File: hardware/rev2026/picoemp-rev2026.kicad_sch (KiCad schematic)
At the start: 47 parts, among them J1 Header 7, J2 1x2_Pin_Header, J3 BG306-02-A-2-0400-L-G, J4 Header 2, J5 Header 4, J6 EDGE-SMA, Q1 LDA111STR, Q2 RGT16BM65DTL, Q3 AO3422, Q4 AO3422, SW1 KSC741J LFS, SW2 KSC741J LFS, SW3 TL3301AF160QJ, T1 ATB322524, T2 ATB322524, U1 SC0915

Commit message: Restore upstream designators and fix header pitch to 2.54mm
The port had P1/P2/P3 replaced by 1.00mm and 1.27mm headers - a 2-2.5x
pitch error on every one. Restoring upstream designators keeps
BUILD-DRAWING-REV04.PDF and the README BOM explainer applicable.

Renames (verified to move zero netlist connections via before/after
membership comparison): LED1/2/3 -> D6/D8/D9, J1/J4/J5 (headers) ->
P1/P2/P3, J6 (SMA) -> J1. Headers get 2.54mm-pitch footprints. Cleared
stale DNP/in_bom=no flags on P1/P2/P3/J2/J3 left over from the
half-finished port.

SW1-3 get footprints: SW1/SW2 share KiCad's stock
Button_Switch_SMD:SW_Push_1P1T_NO_CK_KSC7xxJ land (C&K KSC741JLFS).
SW3 (E-Switch TL3301AF160QJ) gets its own project-local footprint
instead: despite upstream calling it a "shared footprint" part, the
datasheets disagree materially (4.50mm pin pitch vs the KSC7xxJ land's
4.00mm, a 12.5% mismatch).

Backfills the last three missing MPNs (D6/D9 -> APT1608SURCK, the
DigiKey-named substitute for the obsolete APT1608SRCPRV; SW1/SW2 ->
KSC741JLFS; SW3 -> TL3301AF160QJ) with Manufacturer/DigiKey via the
kicad-happy bom skill's edit_properties.py.

Co-Authored-By: Claude Opus 5 <noreply@anthropic.com>
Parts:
- D6: renamed from LED1; DigiKey (none) -> 754-1123-1-ND; MPN (none) -> APT1608SURCK; Manufacturer (none) -> Kingbright
- D9: renamed from LED3; DigiKey (none) -> 754-1123-1-ND; MPN (none) -> APT1608SURCK; Manufacturer (none) -> Kingbright
- J2, J3: now fitted; now in the parts list
- P1: renamed from J1; footprint Connector_PinHeader_1.00mm:PinHeader_1x07_P1.00mm_Vertical -> Connector_PinHeader_2.54mm:PinHeader_1x07_P2.54mm_Vertical; now fitted; now in the parts list
- P2: renamed from J4; footprint Connector_PinHeader_1.27mm:PinHeader_1x02_P1.27mm_Vertical -> Connector_PinHeader_2.54mm:PinHeader_1x02_P2.54mm_Vertical; now fitted; now in the parts list
- P3: renamed from J5; footprint Connector_PinHeader_1.00mm:PinHeader_1x04_P1.00mm_Vertical -> Connector_PinHeader_2.54mm:PinHeader_1x04_P2.54mm_Vertical; now fitted; now in the parts list
- SW1, SW2: footprint (none) -> Button_Switch_SMD:SW_Push_1P1T_NO_CK_KSC7xxJ; DigiKey (none) -> CKN10309CT-ND; MPN (none) -> KSC741JLFS; Manufacturer (none) -> C&K
- SW3: footprint (none) -> picoemp:SW_Push_ESwitch_TL3301AJ; DigiKey (none) -> EG4374CT-ND; MPN (none) -> TL3301AF160QJ; Manufacturer (none) -> E-Switch
- renumbered LED2 to D8, J6 to J1
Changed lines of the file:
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@@
 		(body_style 1)
 		(exclude_from_sim no)
-		(in_bom no)
+		(in_bom yes)
 		(on_board yes)
 		(in_pos_files yes)
-		(dnp yes)
+		(dnp no)
 		(fields_autoplaced yes)
-		(property "Reference" "J1"
+		(property "Reference" "P1"
 			(at 66.675 76.2 0)
 			(show_name no)
@@
 			)
 		)
-		(property "Footprint" "Connector_PinHeader_1.00mm:PinHeader_1x07_P1.00mm_Vertical"
+		(property "Footprint" "Connector_PinHeader_2.54mm:PinHeader_1x07_P2.54mm_Vertical"
 			(at 66.04 86.36 0)
 			(hide yes)
@@
 			(project "ChipShouter-Pico"
 				(path "/2587a454-e9b8-4dd2-940e-91a5ec62d2c9"
-					(reference "J1")
+					(reference "P1")
 					(unit 1)
 				)
@@
 			)
 		)
-		(property "Footprint" ""
+		(property "Footprint" "picoemp:SW_Push_ESwitch_TL3301AJ"
 			(at 347.98 215.9 0)
 			(hide yes)
@@
 			)
 		)
+		(property "DigiKey" "EG4374CT-ND" (at 0 0 0)
+			(effects
+				(font
+					(size 1.27 1.27)
+				)
+				(hide yes)
+			)
+		)
+		(property "Manufacturer" "E-Switch" (at 0 0 0)
+			(effects
+				(font
+					(size 1.27 1.27)
+				)
+				(hide yes)
+			)
+		)
+		(property "MPN" "TL3301AF160QJ" (at 0 0 0)
+			(effects
+				(font
+					(size 1.27 1.27)
+				)
+				(hide yes)
+			)
+		)
 		(pin "1"
 		)
@@
 			)
 		)
-		(property "Footprint" ""
+		(property "Footprint" "Button_Switch_SMD:SW_Push_1P1T_NO_CK_KSC7xxJ"
 			(at 83.82 148.59 0)
 			(hide yes)
@@
 			)
 		)
+		(property "DigiKey" "CKN10309CT-ND" (at 0 0 0)
+			(effects
+				(font
+					(size 1.27 1.27)
+				)
+				(hide yes)
+			)
+		)
+		(property "Manufacturer" "C&K" (at 0 0 0)
+			(effects
+				(font
+					(size 1.27 1.27)
+				)
+				(hide yes)
+			)
+		)
+		(property "MPN" "KSC741JLFS" (at 0 0 0)
+			(effects
+				(font
+					(size 1.27 1.27)
+				)
+				(hide yes)
+			)
+		)
 		(pin "2"
 		)
@@
 			)
 		)
-		(property "Footprint" ""
+		(property "Footprint" "Button_Switch_SMD:SW_Push_1P1T_NO_CK_KSC7xxJ"
 			(at 238.76 127 0)
 			(hide yes)
@@
 			)
 		)
+		(property "DigiKey" "CKN10309CT-ND" (at 0 0 0)
+			(effects
+				(font
+					(size 1.27 1.27)
+				)
+				(hide yes)
+			)
+		)
+		(property "Manufacturer" "C&K" (at 0 0 0)
+			(effects
+				(font
+					(size 1.27 1.27)
+				)
+				(hide yes)
+			)
+		)
+		(property "MPN" "KSC741JLFS" (at 0 0 0)
+			(effects
+				(font
+					(size 1.27 1.27)
+				)
+				(hide yes)
+			)
+		)
 		(pin "1"
 		)
@@
 		(dnp no)
 		(fields_autoplaced yes)
-		(property "Reference" "LED3"
+		(property "Reference" "D9"
 			(at 235.2675 106.68 0)
 			(show_name no)
@@
 			)
 		)
+		(property "DigiKey" "754-1123-1-ND" (at 0 0 0)
+			(effects
+				(font
+					(size 1.27 1.27)
+				)
+				(hide yes)
+			)
+		)
+		(property "Manufacturer" "Kingbright" (at 0 0 0)
+			(effects
+				(font
+					(size 1.27 1.27)
+				)
+				(hide yes)
+			)
+		)
+		(property "MPN" "APT1608SURCK" (at 0 0 0)
+			(effects
+				(font
+					(size 1.27 1.27)
+				)
+				(hide yes)
+			)
+		)
 		(pin "2"
 		)
@@
 			(project "ChipShouter-Pico"
 				(path "/2587a454-e9b8-4dd2-940e-91a5ec62d2c9"
-					(reference "LED3")
+					(reference "D9")
 					(unit 1)
 				)
@@
 		(dnp no)
 		(fields_autoplaced yes)
-		(property "Reference" "LED2"
+		(property "Reference" "D8"
 			(at 64.4525 125.73 0)
 			(show_name no)
@@
 			(project "ChipShouter-Pico"
 				(path "/2587a454-e9b8-4dd2-940e-91a5ec62d2c9"
-					(reference "LED2")
+					(reference "D8")
 					(unit 1)
 				)
@@
 		(dnp no)
 		(fields_autoplaced yes)
-		(property "Reference" "LED1"
+		(property "Reference" "D6"
 			(at 64.4525 110.49 0)
 			(show_name no)
@@
 			)
 		)
+		(property "DigiKey" "754-1123-1-ND" (at 0 0 0)
+			(effects
+				(font
+					(size 1.27 1.27)
+				)
+				(hide yes)
+			)
+		)
+		(property "Manufacturer" "Kingbright" (at 0 0 0)
+			(effects
+				(font
+					(size 1.27 1.27)
+				)
+				(hide yes)
+			)
+		)
+		(property "MPN" "APT1608SURCK" (at 0 0 0)
+			(effects
+				(font
+					(size 1.27 1.27)
+				)
+				(hide yes)
+			)
+		)
 		(pin "2"
 		)
@@
 			(project "ChipShouter-Pico"
 				(path "/2587a454-e9b8-4dd2-940e-91a5ec62d2c9"
-					(reference "LED1")
+					(reference "D6")
 					(unit 1)
 				)
@@
 		(body_style 1)
 		(exclude_from_sim no)
-		(in_bom no)
+		(in_bom yes)
 		(on_board yes)
 		(in_pos_files yes)
-		(dnp yes)
+		(dnp no)
 		(fields_autoplaced yes)
-		(property "Reference" "J4"
+		(property "Reference" "P2"
 			(at 59.69 208.2801 0)
 			(hide yes)
@@
 			)
 		)
-		(property "Footprint" "Connector_PinHeader_1.27mm:PinHeader_1x02_P1.27mm_Vertical"
+		(property "Footprint" "Connector_PinHeader_2.54mm:PinHeader_1x02_P2.54mm_Vertical"
 			(at 58.42 205.74 0)
 			(hide yes)
@@
 			(project "ChipShouter-Pico"
 				(path "/2587a454-e9b8-4dd2-940e-91a5ec62d2c9"
-					(reference "J4")
+					(reference "P2")
 					(unit 1)
 				)
@@
 		(body_style 1)
 		(exclude_from_sim no)
-		(in_bom no)
+		(in_bom yes)
 		(on_board yes)
 		(in_pos_files yes)
-		(dnp yes)
+		(dnp no)
 		(fields_autoplaced yes)
 		(property "Reference" "J2"
@@
 		(dnp no)
 		(fields_autoplaced yes)
-		(property "Reference" "J6"
+		(property "Reference" "J1"
 			(at 420.624 270.51 90)
 			(show_name no)
@@
 			(project "ChipShouter-Pico"
 				(path "/2587a454-e9b8-4dd2-940e-91a5ec62d2c9"
-					(reference "J6")
+					(reference "J1")
 					(unit 1)
 				)
@@
 		(body_style 1)
 		(exclude_from_sim no)
-		(in_bom no)
+		(in_bom yes)
 		(on_board yes)
 		(in_pos_files yes)
-		(dnp yes)
+		(dnp no)
 		(fields_autoplaced yes)
 		(property "Reference" "J3"
@@
 		(body_style 1)
 		(exclude_from_sim no)
-		(in_bom no)
+		(in_bom yes)
 		(on_board yes)
 		(in_pos_files yes)
-		(dnp yes)
+		(dnp no)
 		(fields_autoplaced yes)
-		(property "Reference" "J5"
+		(property "Reference" "P3"
 			(at 99.06 210.8201 0)
 			(hide yes)
@@
 			)
 		)
-		(property "Footprint" "Connector_PinHeader_1.00mm:PinHeader_1x04_P1.00mm_Vertical"
+		(property "Footprint" "Connector_PinHeader_2.54mm:PinHeader_1x04_P2.54mm_Vertical"
 			(at 97.79 208.28 0)
 			(hide yes)
@@
 			(project "ChipShouter-Pico"
 				(path "/2587a454-e9b8-4dd2-940e-91a5ec62d2c9"
-					(reference "J5")
+					(reference "P3")
 					(unit 1)
 				)

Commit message: Add buffered trigger front-end, widen J3, gate on ERC and netlist parity
Trigger input gains a 74LVC1G17 Schmitt buffer (5.5V tolerant), series
and pulldown resistors, and a DNP bypass. J3 moves to 5.08mm: its
2.07mm pad gap failed IEC 60664-1 creepage at ~600V and the BG306's
500VAC rating is a proof test, not a working rating.

- U2 = Nexperia 74LVC1G17GV,125 (SOT-23-5), pinout verified against both
  the Nexperia and TI datasheets (1=NC, 2=A, 3=GND, 4=Y, 5=VCC).
- J3 = Phoenix Contact MKDS 1,5/2-5.08 terminal block (DigiKey 277-1263-ND).
- Pre-existing GND/AGND pin_to_pin ERC error resolved via a UUID-targeted
  erc_exclusions entry in the project file (not a net-tie or global
  severity change).
- 48 tests passing (0 failed); kicad-cli sch erc --severity-error
  --exit-code-violations exits 0.

Co-Authored-By: Claude Opus 5 <noreply@anthropic.com>
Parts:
- added C6: 100n, Capacitor_SMD:C_0603_1608Metric, symbol Device:C_Small
- added J4: EDGE-SMA, Connector_Coaxial:SMA_Amphenol_132289_EdgeMount, symbol Connector:Conn_Coaxial_Power
- added R14: 100R, Resistor_SMD:R_0603_1608Metric, symbol Device:R_Small
- added R15: 10k, Resistor_SMD:R_0603_1608Metric, symbol Device:R_Small
- added R16: 0R, Resistor_SMD:R_0603_1608Metric, symbol Device:R_Small
- added U2: 74LVC1G17, Package_TO_SOT_SMD:SOT-23-5, symbol 74xGxx:74LVC1G17
- J3: value BG306-02-A-2-0400-L-G -> MKDS 1,5/2-5.08; footprint (none) -> TerminalBlock_Phoenix:TerminalBlock_Phoenix_MKDS-1,5-2-5.08_1x02_P5.08mm_Horizontal; BOM Comments (none) -> HV calibration tap. Milled slot between pads - see spec sec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; DigiKey (none) -> 277-1263-ND; MPN (none) -> 1715721; Manufacturer (none) -> Phoenix Contact
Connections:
- net +3V3: now also C6.1, U2.5 (VCC)
- net GND: now also C6.2, J4.2 (Ext), R15.2, U2.3 (GND)
- net GP0: now reaches U1.1 (GPIO0)
- net GP0: now also R16.2, U2.4; no longer P1.1 (Pin_1)
- new net TRIG_BUF: R14.2, R15.1, R16.1, U2.2
- new net TRIG_IN: J4.1 (In), P1.1 (Pin_1), R14.1

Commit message: Lay out the trigger front-end, add HV netclass, start the board
Schematic: trigger front-end placed and wired. Verified against the
exported netlist - /TRIG_IN {P1.1, J4.1, R14.1}, /TRIG_BUF {R14.2,
R15.1, R16.1, U2.2}, /GP0 {R16.2, U1.1, U2.4} with no P1.1 member,
U2.5 on +3V3 and U2.3 on GND. ERC exits 0, 54 tests pass.

Board setup: min_clearance 0.0 -> 0.2 (it was enforcing nothing on a
board that generates ~500V), plus an HV netclass at 0.75mm assigned by
explicit pattern to the seven HV nets.

The 0.75mm is measured, not chosen. Pad geometry on the hi-pot-validated
original board gives 0.770mm at T1's own primary-to-secondary spacing
and ~1.002mm in routed copper; 0.75 sits just under the part-imposed
floor so T1/T2's own pads don't false-flag every DRC run.

The old board's NET LABELS could not be used for this - a track labelled
NetQ1_1 terminates on a pad labelled NetJ3_2, and R1's pad-to-net
assignment is reversed between its legacy and new footprints. The
measurement uses pad geometry classified by component instead, and
excludes Q1 whose imported footprint has fused pads.

tests/test_board_setup.py locks all of the above, since KiCad rewrites
.kicad_pro on every save.

Board file created: 1.6mm thickness (the edge-mount SMA clamps the board
edge), Edge.Cuts imported at 40.00 x 116.00mm. No footprints yet.

Co-Authored-By: Claude Opus 5 <noreply@anthropic.com>
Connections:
- net GP0: now also R16.1; no longer R16.2
- net TRIG_BUF: now also R16.2; no longer R16.1
- net STATUS_LED: now reaches R12.1, U1.10 (GPIO7)
- net CHARGE_LED: now reaches R13.1, U1.32 (GPIO27_ADC1)
- net GP1: now reaches P1.2 (Pin_2), U1.2 (GPIO1)
- net GP2: now reaches P1.3 (Pin_3), U1.4 (GPIO2)
- net GP3: now reaches P1.4 (Pin_4), U1.5 (GPIO3)
- net GP4: now reaches P1.5 (Pin_5), U1.6 (GPIO4)
- net GP5: now reaches P1.6 (Pin_6), U1.7 (GPIO5)
- net PULSE_SW: now reaches SW2.1, U1.15 (GPIO11)
- net ARM_SW: now reaches SW1.1, U1.34 (GPIO28_ADC2)
- net HV_DET_LED: now reaches R11.1, U1.9 (GPIO6)
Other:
- note added: "High Voltage Side"
- note added: "MCU"
- note added: "Physical"
- note added: "Trigger Buffer"
- moved on the sheet: C6, J4, R14, R15, R16, U2

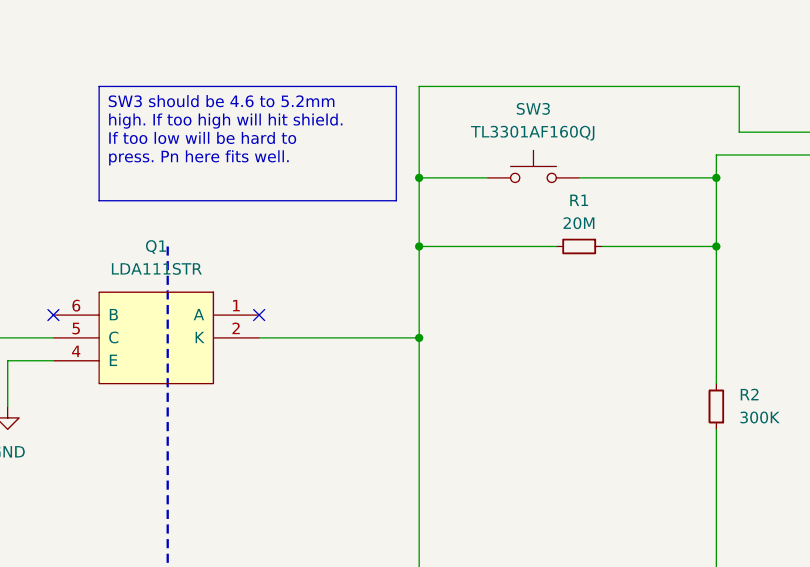
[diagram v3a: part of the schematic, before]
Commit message: Fix Q1 optocoupler LED feedback path (floating anode from Altium import)
Q1 (LDA111) pin 1, the LED anode, had a no_connect flag left over from the
Altium->KiCad import, and R1's free end ran straight into Net-(D7-A) (the
HV return) instead of into Q1 pin 1. This shorted the feedback LED out of
the circuit: no LED current, phototransistor never conducts, /CHARGED
never asserts.

Rewired R1's free pin to Q1 pin 1 (HV+ -> R2 -> tap -> R1 -> Q1.1 LED
anode; Q1.2 LED cathode stays on the HV return with Q2.3). Verified via
netlist membership diff that this is the only change: Q1.1 moves off its
unconnected-* net onto a new net with R1's free pin, and Net-(D7-A) loses
exactly that one R1 member -- nothing else moved. ERC is clean.

Added test_hv_charge_feedback_led_path_intact to tests/test_netlist.py,
asserting the feedback path by pin co-membership (orientation-agnostic on
which R1 pin faces the tap). Verified the test has teeth by reverting the
wiring in a scratch copy and confirming it (and only it) fails.

Co-Authored-By: Claude Opus 5 <noreply@anthropic.com>
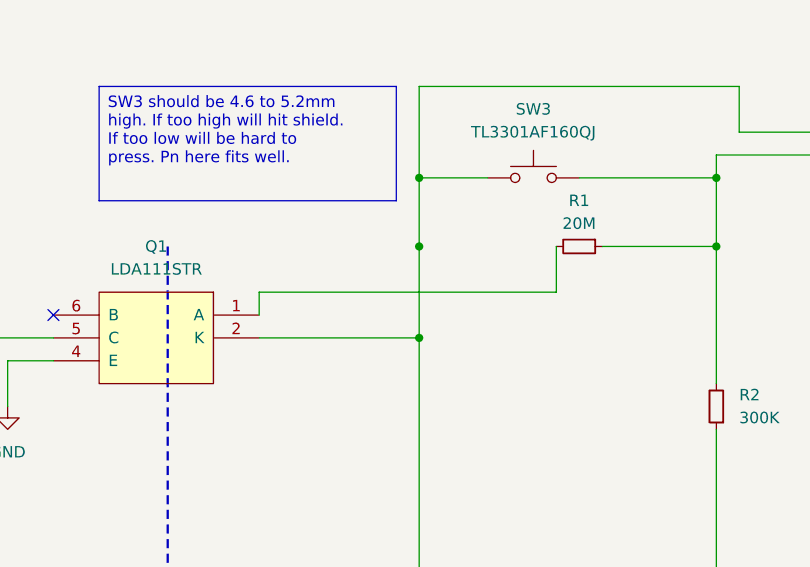
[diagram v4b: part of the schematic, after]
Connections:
- net at C3.1, D7.2 (A), J3.1 (Pin_1)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: no longer R1.2
- net at Q1.1 (A): now also R1.2
- no-connect marks 27 -> 26
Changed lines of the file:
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@@
-	)
-	(no_connect
-		(at 317.5 236.22)
 	)
 	(no_connect
@@
 	(wire
 		(pts
-			(xy 335.28 228.6) (xy 350.52 228.6)
-		)
-		(stroke
+			(xy 350.52 228.6) (xy 350.52 233.68)
+		)
+		(stroke
+			(width 0)
+			(type default)
+		)
+	)
+	(wire
+		(pts
+			(xy 317.5 233.68) (xy 350.52 233.68)
+		)
+		(stroke
+			(width 0)
+			(type default)
+		)
+	)
+	(wire
+		(pts
+			(xy 317.5 233.68) (xy 317.5 236.22)
+		)
+		(stroke
